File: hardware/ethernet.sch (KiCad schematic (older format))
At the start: 62 parts, among them IC201 MAX5969x, IC202 KSZ8081RNA, IC203 MAX17503, J201 RJ45, J202 AUX POWER, T201 749010012A, Y201 25MHz

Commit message: various routing
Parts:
- removed TP203: 25MHz_XTAL, agg:TESTPAD, symbol TESTPAD
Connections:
- net 3v3: no longer C217.1, C218.1
- net at IC202.2 (VDDA_3v3), L202.2: now also C217.1, C218.1
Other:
- note removed: "VDDA\nDECOUPLING"
- note removed: "VDDIO\nDECOUPLING"
- moved on the sheet: C214, C216, C217, C218, L202
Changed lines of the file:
@@
 L 3v3 #PWR064
 U 1 1 57F0D67E
-P 6500 900
-F 0 "#PWR064" H 6500 1010 50  0001 L CNN
-F 1 "3v3" H 6500 990 50  0000 C CNN
-F 2 "" H 6500 900 60  0001 C CNN
-F 3 "" H 6500 900 60  0001 C CNN
-	1    6500 900
+P 5450 650
+F 0 "#PWR064" H 5450 760 50  0001 L CNN
+F 1 "3v3" H 5450 740 50  0000 C CNN
+F 2 "" H 5450 650 60  0001 C CNN
+F 3 "" H 5450 650 60  0001 C CNN
+	1    5450 650
 	1    0    0    -1
 $EndComp
@@
 L L_Small L202
 U 1 1 57F0D79F
-P 6750 900
-F 0 "L202" H 6780 940 50  0000 L CNN
-F 1 "FB" H 6780 860 50  0000 L CNN
-F 2 "agg:0603" H 6750 900 50  0001 C CNN
-F 3 "http://www.farnell.com/datasheets/2005683.pdf" H 6750 900 50  0001 C CNN
-F 4 "1463451" H 6750 900 60  0001 C CNN "Farnell"
-	1    6750 900
-	0    -1   -1   0
+P 5000 800
+F 0 "L202" H 5030 840 50  0000 L CNN
+F 1 "FB" H 5030 760 50  0000 L CNN
+F 2 "agg:0603" H 5000 800 50  0001 C CNN
+F 3 "http://www.farnell.com/datasheets/2005683.pdf" H 5000 800 50  0001 C CNN
+F 4 "1463451" H 5000 800 60  0001 C CNN "Farnell"
+	1    5000 800
+	1    0    0    -1
 $EndComp
 $Comp
 L C C216
 U 1 1 57F0D9DD
-P 7150 3050
-F 0 "C216" H 7175 3150 50  0000 L CNN
-F 1 "100n" H 7200 2950 50  0000 L CNN
-F 2 "agg:0603" H 7188 2900 50  0001 C CNN
-F 3 "http://www.farnell.com/datasheets/2121819.pdf" H 7150 3050 50  0001 C CNN
-F 4 "1650835" H 7150 3050 60  0001 C CNN "Farnell"
-	1    7150 3050
+P 5900 1150
+F 0 "C216" H 5925 1250 50  0000 L CNN
+F 1 "100n" H 5950 1050 50  0000 L CNN
+F 2 "agg:0603" H 5938 1000 50  0001 C CNN
+F 3 "http://www.farnell.com/datasheets/2121819.pdf" H 5900 1150 50  0001 C CNN
+F 4 "1650835" H 5900 1150 60  0001 C CNN "Farnell"
+	1    5900 1150
 	1    0    0    -1
 $EndComp
@@
 L C C214
 U 1 1 57F0E24C
-P 6900 3050
-F 0 "C214" H 6925 3150 50  0000 L CNN
-F 1 "22u" H 6925 2950 50  0000 L CNN
-F 2 "agg:1206" H 6938 2900 50  0001 C CNN
-F 3 "http://www.farnell.com/datasheets/2048536.pdf" H 6900 3050 50  0001 C CNN
-F 4 "1797010" H 6900 3050 60  0001 C CNN "Farnell"
-	1    6900 3050
-	1    0    0    -1
-$EndComp
-Wire Wire Line
-	6500 900  6650 900
-Wire Wire Line
-	6600 900  6600 1000
-Wire Wire Line
-	6600 1000 6850 1000
-Connection ~ 6600 900
-$Comp
-L 3v3 #PWR065
-U 1 1 57F0FE2E
-P 7050 2850
-F 0 "#PWR065" H 7050 2960 50  0001 L CNN
-F 1 "3v3" H 7050 2940 50  0000 C CNN
-F 2 "" H 7050 2850 60  0001 C CNN
-F 3 "" H 7050 2850 60  0001 C CNN
-	1    7050 2850
-	1    0    0    -1
-$EndComp
-Wire Wire Line
-	7050 2850 7050 2900
-Wire Wire Line
-	6900 2900 7150 2900
-Connection ~ 7050 2900
-$Comp
-L GND #PWR066
-U 1 1 57F10083
-P 7050 3200
-F 0 "#PWR066" H 7050 2950 50  0001 C CNN
-F 1 "GND" H 7050 3050 50  0000 C CNN
-F 2 "" H 7050 3200 50  0000 C CNN
-F 3 "" H 7050 3200 50  0000 C CNN
-	1    7050 3200
-	1    0    0    -1
-$EndComp
-Wire Wire Line
-	6900 3200 7150 3200
-Connection ~ 7050 3200
+P 5650 1150
+F 0 "C214" H 5675 1250 50  0000 L CNN
+F 1 "22u" H 5675 1050 50  0000 L CNN
+F 2 "agg:1206" H 5688 1000 50  0001 C CNN
+F 3 "http://www.farnell.com/datasheets/2048536.pdf" H 5650 1150 50  0001 C CNN
+F 4 "1797010" H 5650 1150 60  0001 C CNN "Farnell"
+	1    5650 1150
+	1    0    0    -1
+$EndComp
+Wire Wire Line
+	4750 900  6850 900
+Wire Wire Line
+	5650 1000 6850 1000
+Wire Wire Line
+	5650 1300 5900 1300
 $Comp
 L C C218
 U 1 1 57F1034A
-P 7850 3050
-F 0 "C218" H 7875 3150 50  0000 L CNN
-F 1 "100n" H 7900 2950 50  0000 L CNN
-F 2 "agg:0603" H 7888 2900 50  0001 C CNN
-F 3 "http://www.farnell.com/datasheets/2121819.pdf" H 7850 3050 50  0001 C CNN
-F 4 "1650835" H 7850 3050 60  0001 C CNN "Farnell"
-	1    7850 3050
-	1    0    0    -1
-$EndComp
-$Comp
-L 3v3 #PWR067
-U 1 1 57F10357
-P 7750 2850
-F 0 "#PWR067" H 7750 2960 50  0001 L CNN
-F 1 "3v3" H 7750 2940 50  0000 C CNN
-F 2 "" H 7750 2850 60  0001 C CNN
-F 3 "" H 7750 2850 60  0001 C CNN
-	1    7750 2850
-	1    0    0    -1
-$EndComp
-Wire Wire Line
-	7750 2850 7750 2900
-Wire Wire Line
-	7600 2900 7850 2900
-Connection ~ 7750 2900
-$Comp
-L GND #PWR068
-U 1 1 57F10360
-P 7750 3200
-F 0 "#PWR068" H 7750 2950 50  0001 C CNN
-F 1 "GND" H 7750 3050 50  0000 C CNN
-F 2 "" H 7750 3200 50  0000 C CNN
-F 3 "" H 7750 3200 50  0000 C CNN
-	1    7750 3200
-	1    0    0    -1
-$EndComp
-Wire Wire Line
-	7600 3200 7850 3200
-Connection ~ 7750 3200
-Text Notes 6750 3600 0    60   ~ 0
-VDDIO\nDECOUPLING
-Text Notes 7500 3600 0    60   ~ 0
-VDDA\nDECOUPLING
+P 5000 1050
+F 0 "C218" H 5025 1150 50  0000 L CNN
+F 1 "100n" H 5050 950 50  0000 L CNN
+F 2 "agg:0603" H 5038 900 50  0001 C CNN
+F 3 "http://www.farnell.com/datasheets/2121819.pdf" H 5000 1050 50  0001 C CNN
+F 4 "1650835" H 5000 1050 60  0001 C CNN "Farnell"
+	1    5000 1050
+	1    0    0    -1
+$EndComp
+Wire Wire Line
+	4750 1200 5000 1200
 $Comp
 L XTAL Y201
@@
 Connection ~ 6600 2200
 $Comp
-L GND #PWR069
+L GND #PWR065
 U 1 1 57F12D2E
 P 6500 2700
-F 0 "#PWR069" H 6500 2450 50  0001 C CNN
+F 0 "#PWR065" H 6500 2450 50  0001 C CNN
 F 1 "GND" H 6500 2550 50  0000 C CNN
 F 2 "" H 6500 2700 50  0000 C CNN
@@
 $EndComp
 $Comp
-L 3v3 #PWR070
+L 3v3 #PWR066
 U 1 1 57F16B5B
 P 8550 1500
-F 0 "#PWR070" H 8550 1610 50  0001 L CNN
+F 0 "#PWR066" H 8550 1610 50  0001 L CNN
 F 1 "3v3" H 8550 1590 50  0000 C CNN
 F 2 "" H 8550 1500 60  0001 C CNN
@@
 	8050 2100 8150 2100
 $Comp
-L GND #PWR071
+L GND #PWR067
 U 1 1 57F1933C
 P 8500 2100
-F 0 "#PWR071" H 8500 1850 50  0001 C CNN
+F 0 "#PWR067" H 8500 1850 50  0001 C CNN
 F 1 "GND" H 8500 1950 50  0000 C CNN
 F 2 "" H 8500 2100 50  0000 C CNN
@@
 Connection ~ 9400 2100
 $Comp
-L 3v3 #PWR072
+L 3v3 #PWR068
 U 1 1 57F1DF9F
 P 9400 2050
-F 0 "#PWR072" H 9400 2160 50  0001 L CNN
+F 0 "#PWR068" H 9400 2160 50  0001 L CNN
 F 1 "3v3" H 9400 2140 50  0000 C CNN
 F 2 "" H 9400 2050 60  0001 C CNN
@@
 $EndComp
 $Comp
-L GND #PWR073
+L GND #PWR069
 U 1 1 57F1E163
 P 9400 2700
-F 0 "#PWR073" H 9400 2450 50  0001 C CNN
+F 0 "#PWR069" H 9400 2450 50  0001 C CNN
 F 1 "GND" H 9400 2550 50  0000 C CNN
 F 2 "" H 9400 2700 50  0000 C CNN
@@
 GND
 $Comp
-L GND #PWR074
+L GND #PWR070
 U 1 1 57F26BFA
 P 9600 4800
-F 0 "#PWR074" H 9600 4550 50  0001 C CNN
+F 0 "#PWR070" H 9600 4550 50  0001 C CNN
 F 1 "GND" H 9600 4650 50  0000 C CNN
 F 2 "" H 9600 4800 50  0000 C CNN
@@
 L C C217
 U 1 1 57F58968
-P 7600 3050
-F 0 "C217" H 7625 3150 50  0000 L CNN
-F 1 "22u" H 7625 2950 50  0000 L CNN
-F 2 "agg:1206" H 7638 2900 50  0001 C CNN
-F 3 "http://www.farnell.com/datasheets/2048536.pdf" H 7600 3050 50  0001 C CNN
-F 4 "1797010" H 7600 3050 60  0001 C CNN "Farnell"
-	1    7600 3050
+P 4750 1050
+F 0 "C217" H 4775 1150 50  0000 L CNN
+F 1 "22u" H 4775 950 50  0000 L CNN
+F 2 "agg:1206" H 4788 900 50  0001 C CNN
+F 3 "http://www.farnell.com/datasheets/2048536.pdf" H 4750 1050 50  0001 C CNN
+F 4 "1797010" H 4750 1050 60  0001 C CNN "Farnell"
+	1    4750 1050
 	1    0    0    -1
 $EndComp
@@
 	6500 2650 6500 2700
 Connection ~ 6500 2650
-Wire Wire Line
-	6800 2300 6800 2500
-Connection ~ 6800 2300
-$Comp
-L TESTPAD TP203
-U 1 1 57F35973
-P 6800 2500
-F 0 "TP203" H 6800 2550 50  0000 L CNN
-F 1 "25MHz_XTAL" H 6800 2425 50  0001 L CNN
-F 2 "agg:TESTPAD" H 6800 2350 50  0001 L CNN
-F 3 "" H 6800 2500 50  0001 C CNN
-	1    6800 2500
-	0    1    1    0
-$EndComp
 $Comp
 L TESTPAD TP204
@@
 Connection ~ 8150 1200
 $Comp
-L PWR #FLG075
+L PWR #FLG071
 U 1 1 57F5C8CD
 P 10350 4550
-F 0 "#FLG075" H 10350 4710 50  0001 C CNN
+F 0 "#FLG071" H 10350 4710 50  0001 C CNN
 F 1 "PWR" H 10350 4640 50  0000 C CNN
 F 2 "" H 10350 4550 50  0001 C CNN
@@
 Connection ~ 10350 4600
 NoConn ~ 1200 2150
+Connection ~ 5800 1000
+Connection ~ 5000 900
+Wire Wire Line
+	5000 650  5800 650
+Wire Wire Line
+	5800 650  5800 1000
+Connection ~ 5450 650
+Wire Wire Line
+	5000 650  5000 700
+Connection ~ 5900 1000
+$Comp
+L GND #PWR072
+U 1 1 57F877E8
+P 4900 1200
+F 0 "#PWR072" H 4900 950 50  0001 C CNN
+F 1 "GND" H 4900 1050 50  0000 C CNN
+F 2 "" H 4900 1200 50  0000 C CNN
+F 3 "" H 4900 1200 50  0000 C CNN
+	1    4900 1200
+	1    0    0    -1
+$EndComp
+Connection ~ 4900 1200
+$Comp
+L GND #PWR073
+U 1 1 57F878B8
+P 5800 1300
+F 0 "#PWR073" H 5800 1050 50  0001 C CNN
+F 1 "GND" H 5800 1150 50  0000 C CNN
+F 2 "" H 5800 1300 50  0000 C CNN
+F 3 "" H 5800 1300 50  0000 C CNN
+	1    5800 1300
+	1    0    0    -1
+$EndComp
+Connection ~ 5800 1300
 $EndSCHEMATC

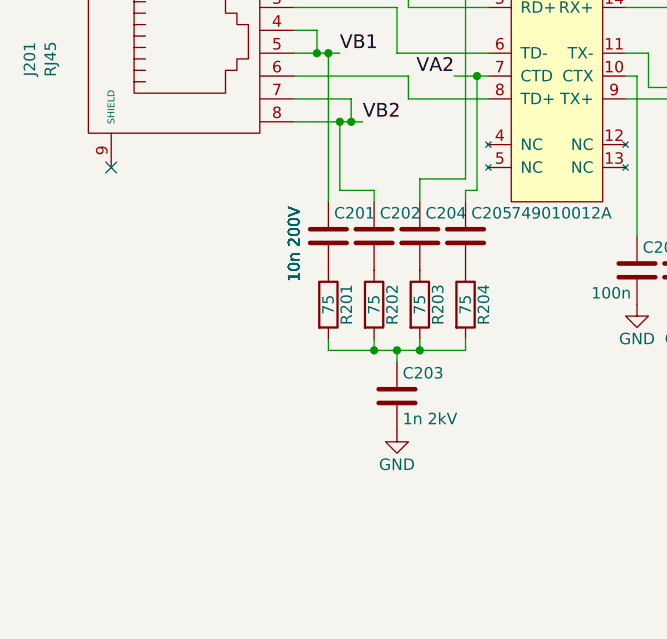
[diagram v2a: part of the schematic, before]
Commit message: Moved Bob Smith from signal gnd to chassis gnd
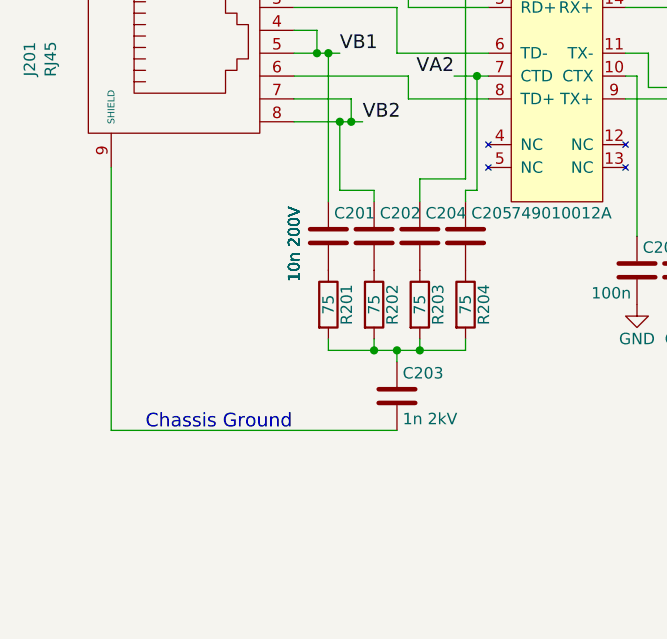
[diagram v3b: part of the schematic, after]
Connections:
- net GND: no longer C203.2
- net at J201.9 (SHIELD): now also C203.2
- no-connect marks 8 -> 7
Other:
- note added: "Chassis Ground"
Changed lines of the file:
@@
 	2150 2900 2150 2950
 Connection ~ 2350 2950
-$Comp
-L GND #PWR058
-U 1 1 57F04B92
-P 2450 3300
-F 0 "#PWR058" H 2450 3050 50  0001 C CNN
-F 1 "GND" H 2450 3150 50  0000 C CNN
-F 2 "" H 2450 3300 50  0000 C CNN
-F 3 "" H 2450 3300 50  0000 C CNN
-	1    2450 3300
-	1    0    0    -1
-$EndComp
 Wire Wire Line
 	3450 1450 4250 1450
@@
 	10350 4550 10350 4600
 Connection ~ 10350 4600
-NoConn ~ 1200 2150
 Connection ~ 5800 1000
 Connection ~ 5000 900
@@
 $EndComp
 Connection ~ 5800 1300
+Wire Wire Line
+	1200 2150 1200 3300
+Wire Wire Line
+	1200 3300 2450 3300
+Text Notes 1350 3300 0    60   ~ 0
+Chassis Ground
 $EndSCHEMATC

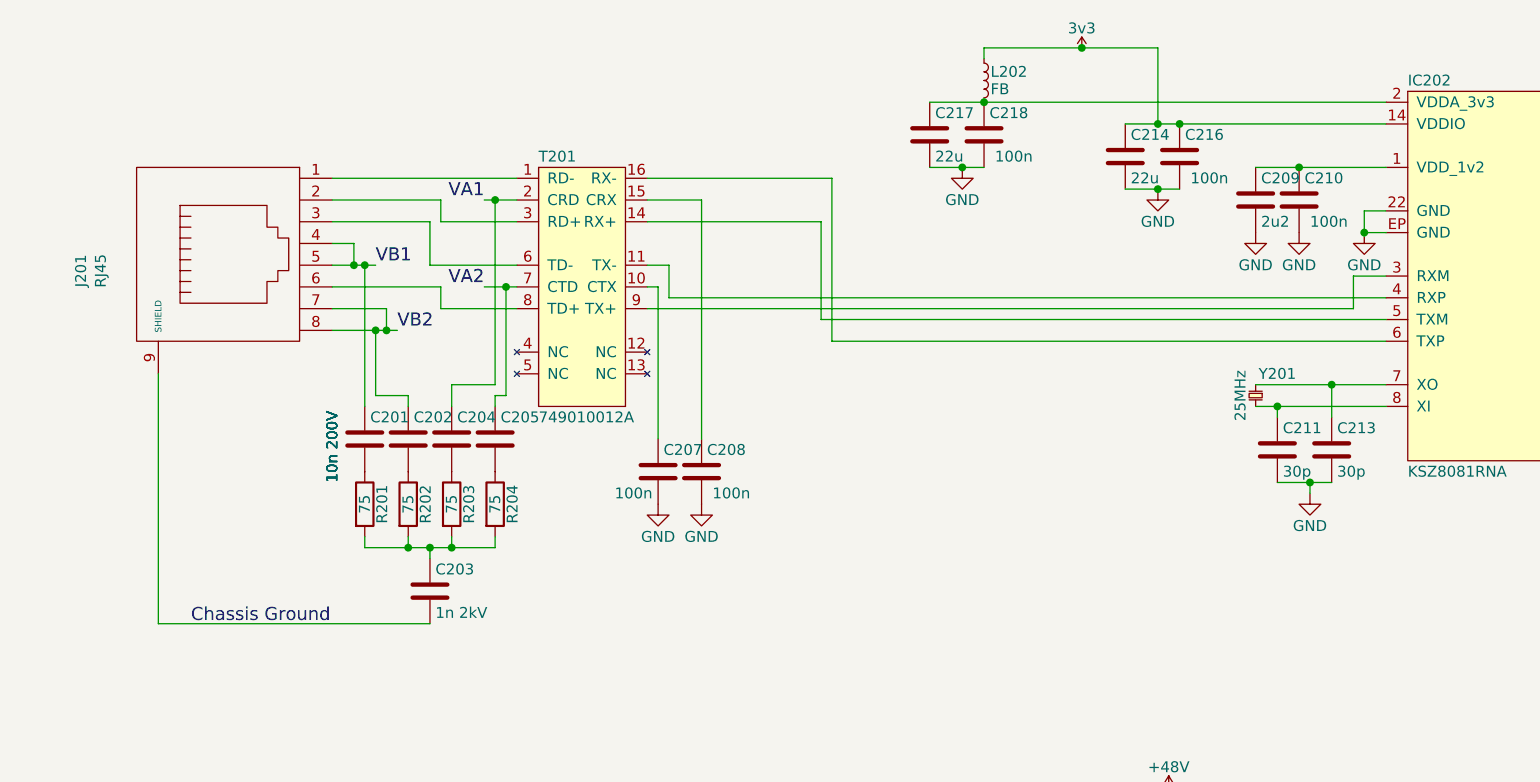
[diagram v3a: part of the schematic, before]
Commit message: Invert ethernet magnetics ordering.
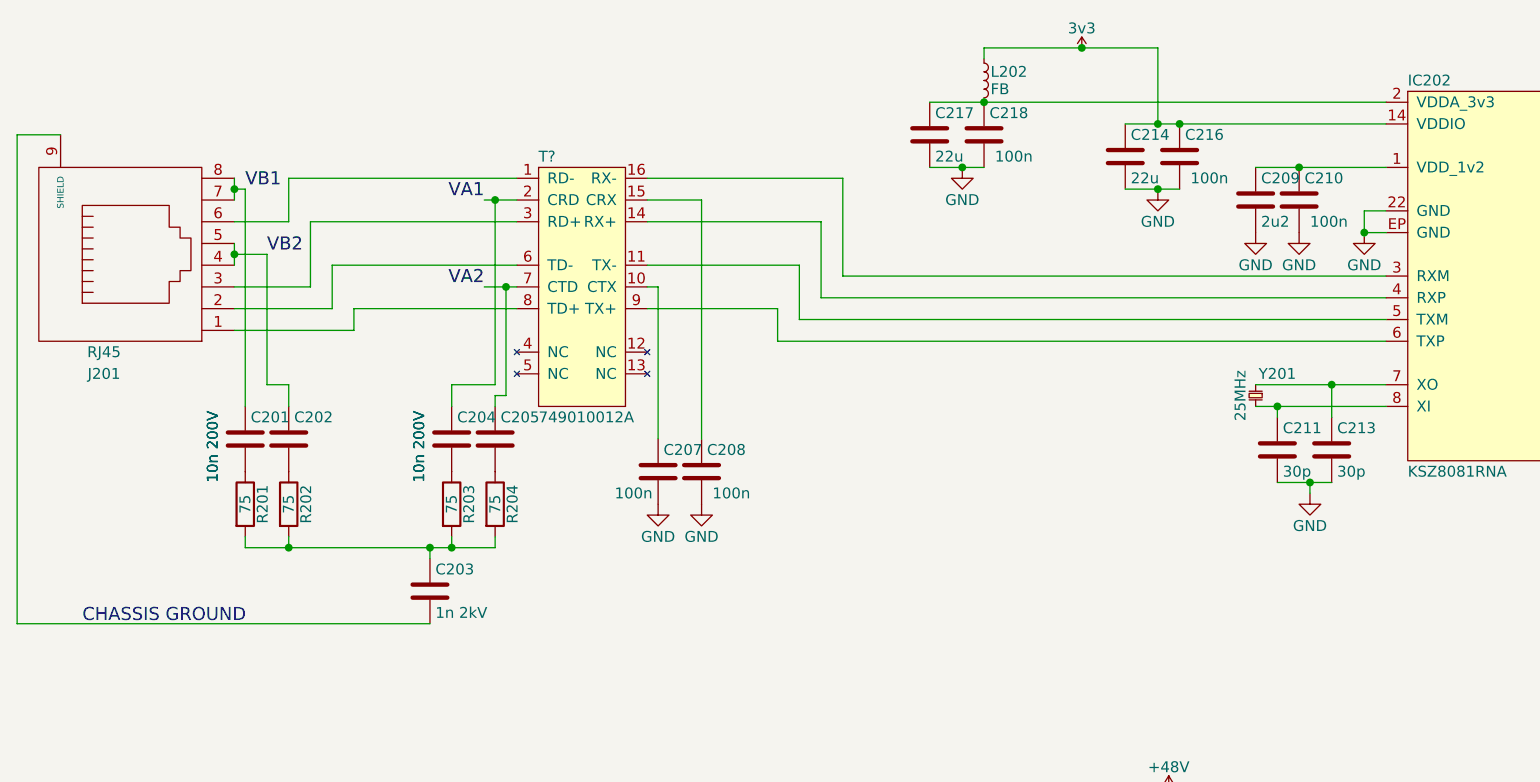
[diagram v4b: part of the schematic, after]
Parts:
- removed T201: 749010012A, agg:749010012A, symbol 749010012A
- added T?: 749010012A, agg:749010012A, symbol 749010012A
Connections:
- net VA1: now also T?.2 (CRD)
- net VA2: now also T?.7 (CTD)
- net VB1: now also J201.7, J201.8; no longer J201.4, J201.5
- net VB2: now also J201.4, J201.5; no longer J201.7, J201.8
- net at J201.1: now also T?.8 (TD+)
- net at J201.2: now also T?.6 (TD-)
- net at J201.3: now also T?.3 (RD+)
- net at J201.6: now also T?.1 (RD-)
- net at C207.1: now also T?.10 (CTX)
- net at IC202.4 (RXP): now also T?.14 (RX+)
- net at IC202.5 (TXM): now also T?.11 (TX-)
- net at C208.1: now also T?.15 (CRX)
- net at IC202.6 (TXP): now also T?.9 (TX+)
- net at IC202.3 (RXM): now also T?.16 (RX-)
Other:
- note added: "CHASSIS GROUND"
- note removed: "Chassis Ground"
- moved on the sheet: C201, C202, J201, R201, R202
